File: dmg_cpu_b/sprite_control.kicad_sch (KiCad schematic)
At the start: 136 parts

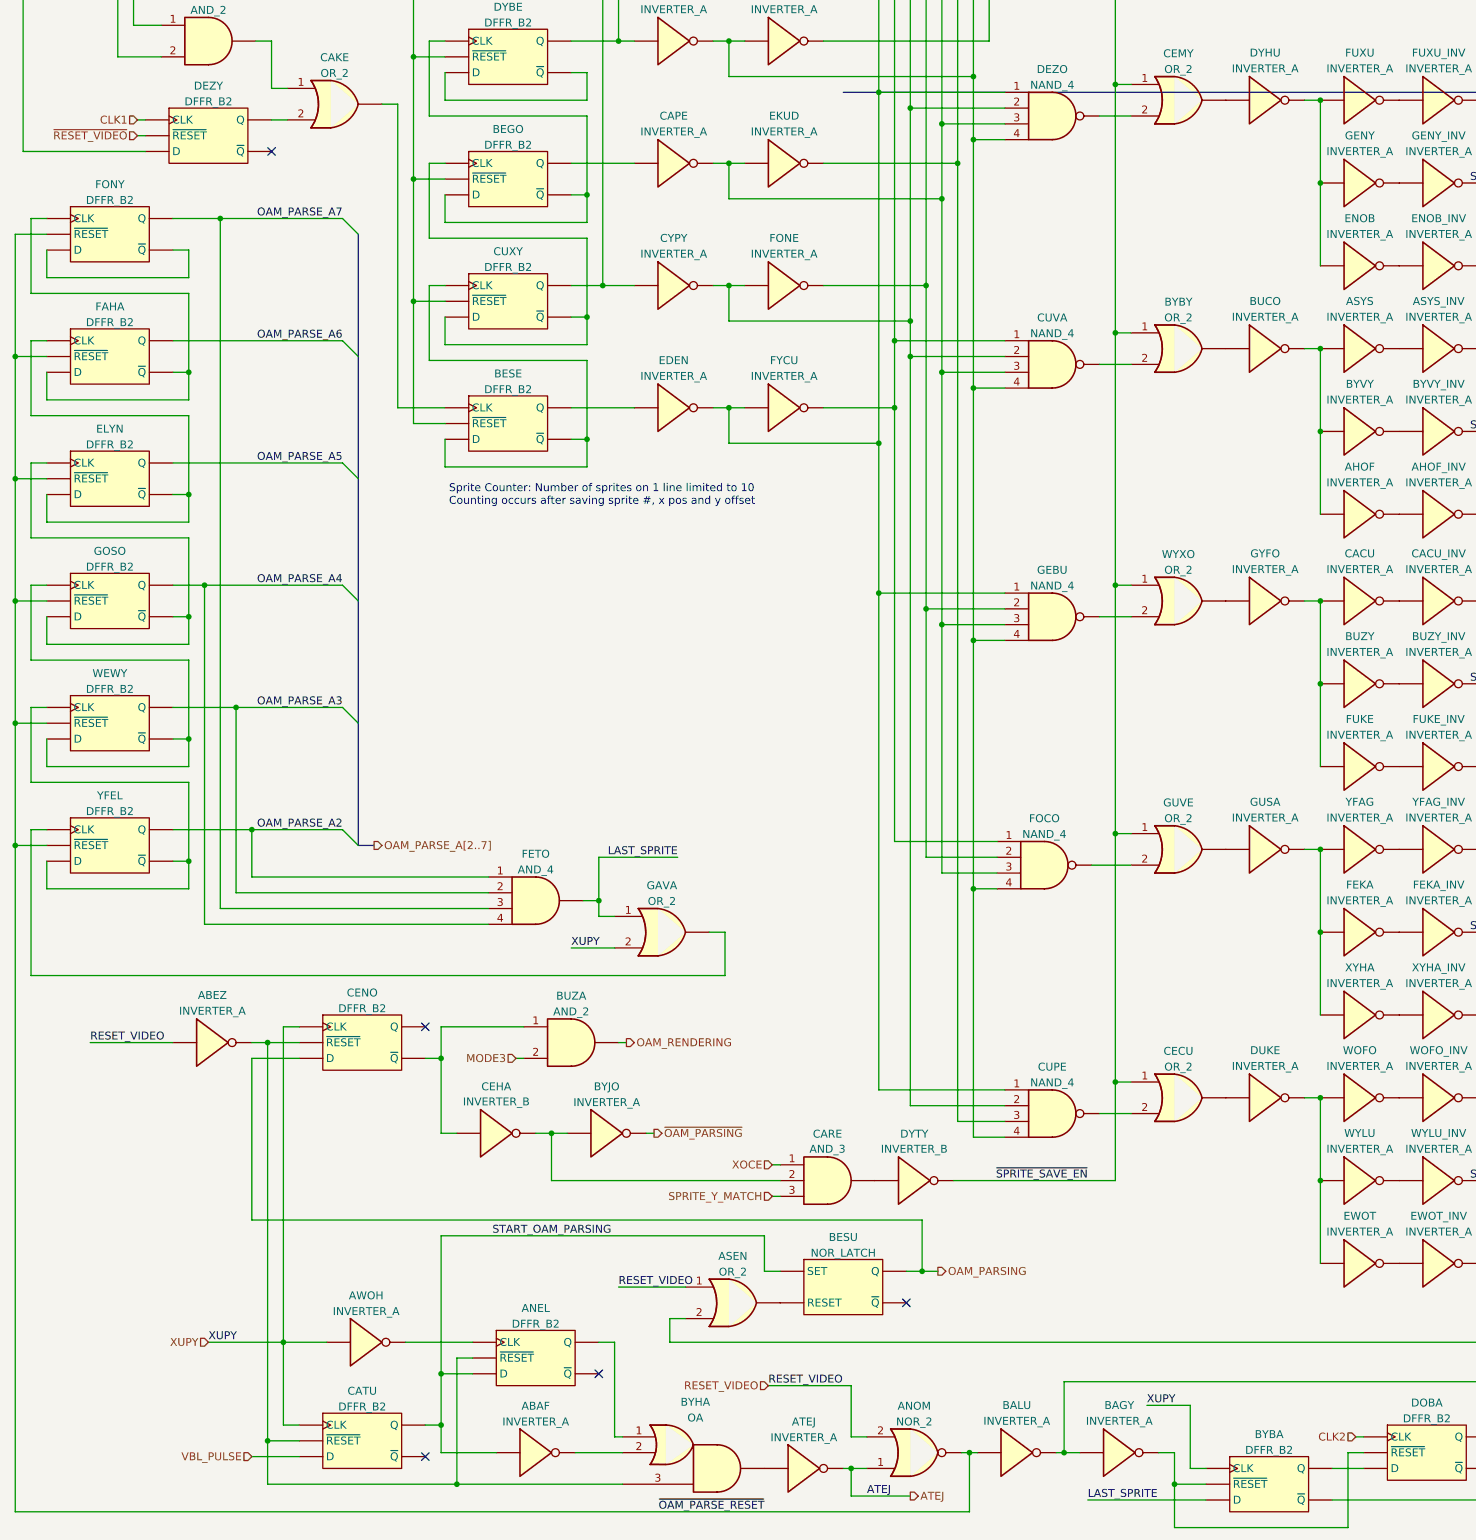
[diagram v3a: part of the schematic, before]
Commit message: PPU hierarchical page progress. Elements moved out of window sheet to be includes in BG and WIN cycles sheet
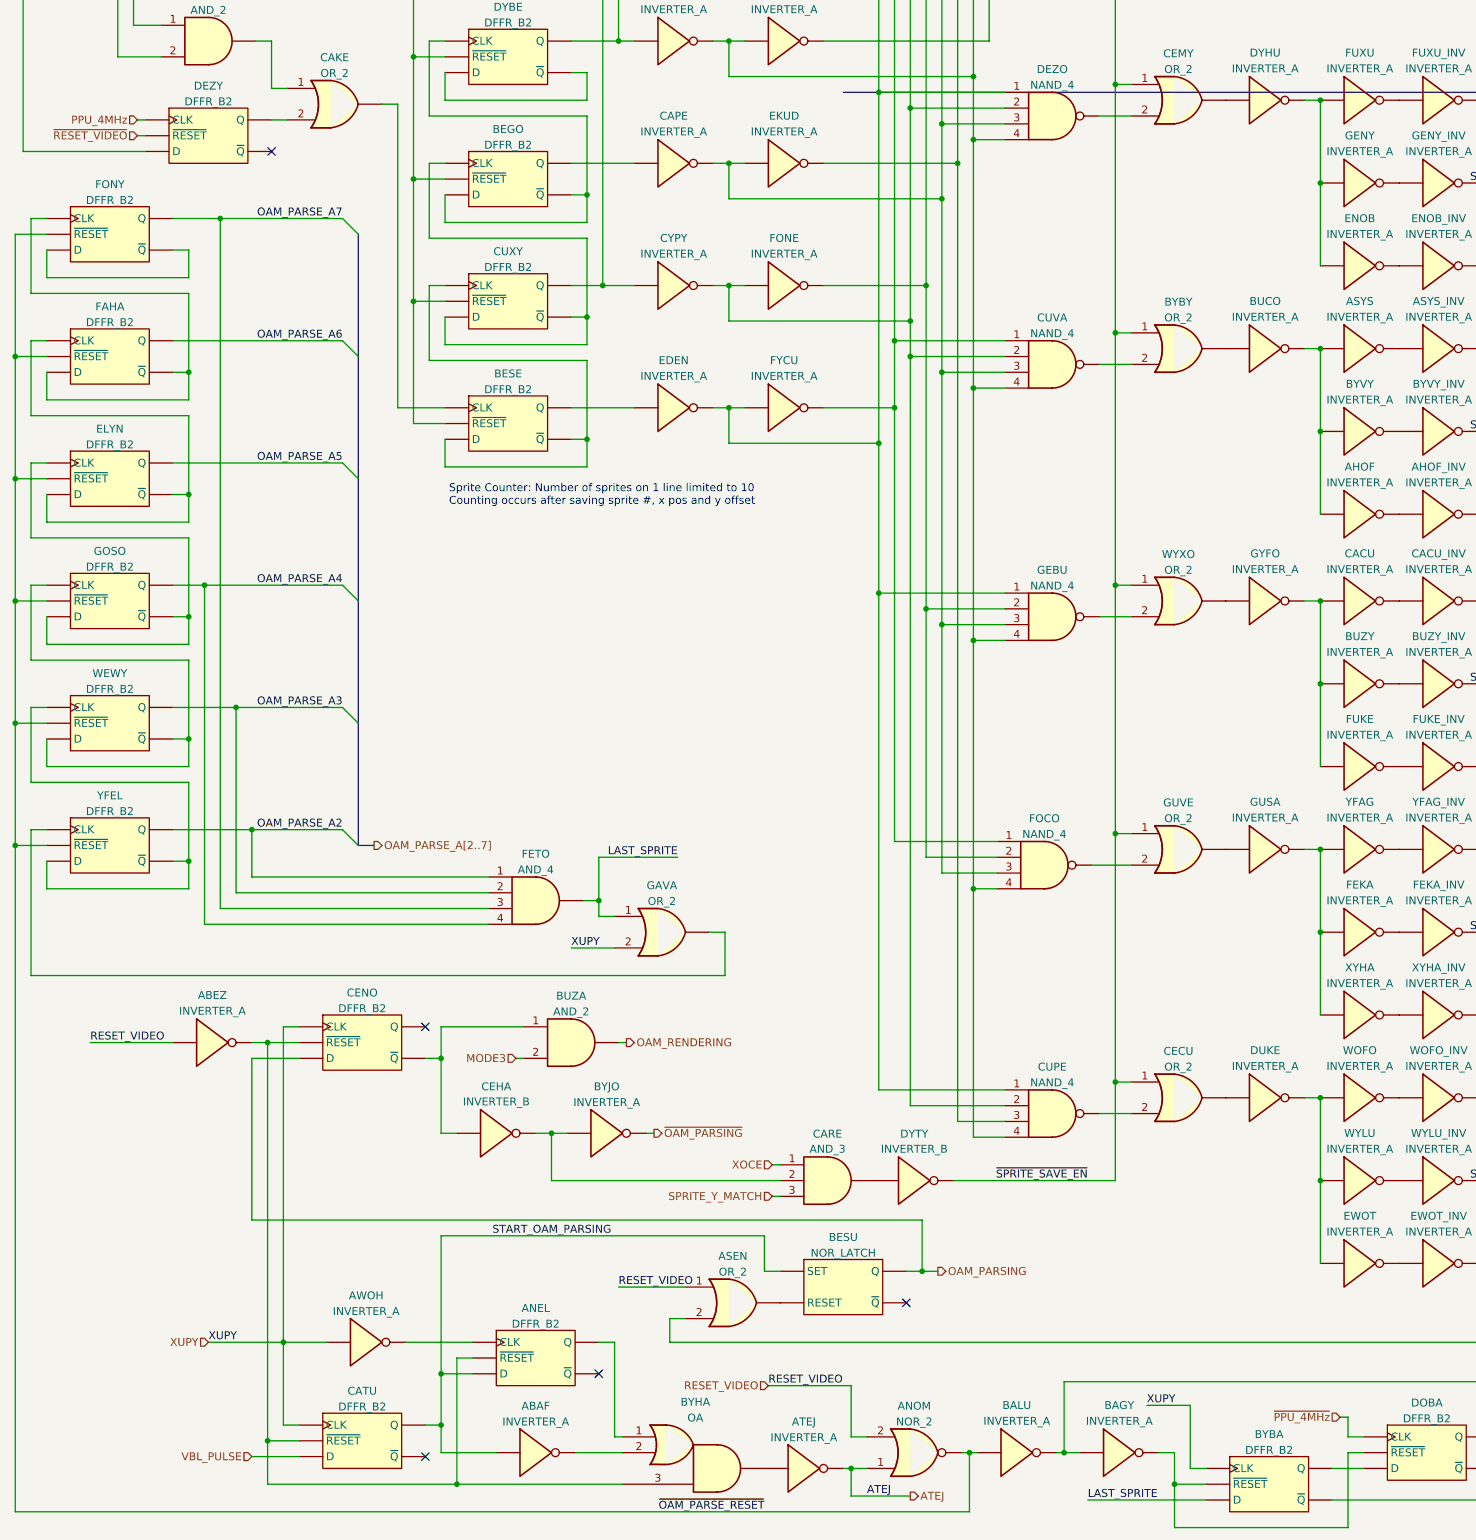
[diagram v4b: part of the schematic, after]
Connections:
- net CLK1 renamed PPU_4MHz
- net CLK2 renamed ~{PPU_4MHz}
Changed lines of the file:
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@@
     (stroke (width 0) (type default) (color 0 0 0 0))
   )
-  (wire (pts (xy 232.41 267.97) (xy 233.68 267.97))
+  (wire (pts (xy 229.87 264.795) (xy 231.14 264.795))
     (stroke (width 0) (type default) (color 0 0 0 0))
   )
@@
     (stroke (width 0) (type default) (color 0 0 0 0))
   )
+  (wire (pts (xy 231.14 267.97) (xy 233.68 267.97))
+    (stroke (width 0) (type default) (color 0 0 0 0))
+  )
   (wire (pts (xy 128.27 186.69) (xy 130.81 186.69))
     (stroke (width 0) (type default) (color 0 0 0 0))
@@
   )
   (bus (pts (xy 400.685 81.915) (xy 400.685 41.91))
+    (stroke (width 0) (type default) (color 0 0 0 0))
+  )
+  (wire (pts (xy 231.14 264.795) (xy 231.14 267.97))
     (stroke (width 0) (type default) (color 0 0 0 0))
   )
@@
     (effects (font (size 1.27 1.27)) (justify right))
   )
-  (hierarchical_label "CLK2" (shape input) (at 232.41 267.97 180)
+  (hierarchical_label "~{PPU_4MHz}" (shape input) (at 229.87 264.795 180)
     (effects (font (size 1.27 1.27)) (justify right))
   )
@@
     (effects (font (size 1.27 1.27)) (justify left))
   )
-  (hierarchical_label "CLK1" (shape input) (at 36.195 55.88 180)
+  (hierarchical_label "PPU_4MHz" (shape input) (at 36.195 55.88 180)
     (effects (font (size 1.27 1.27)) (justify right))
   )

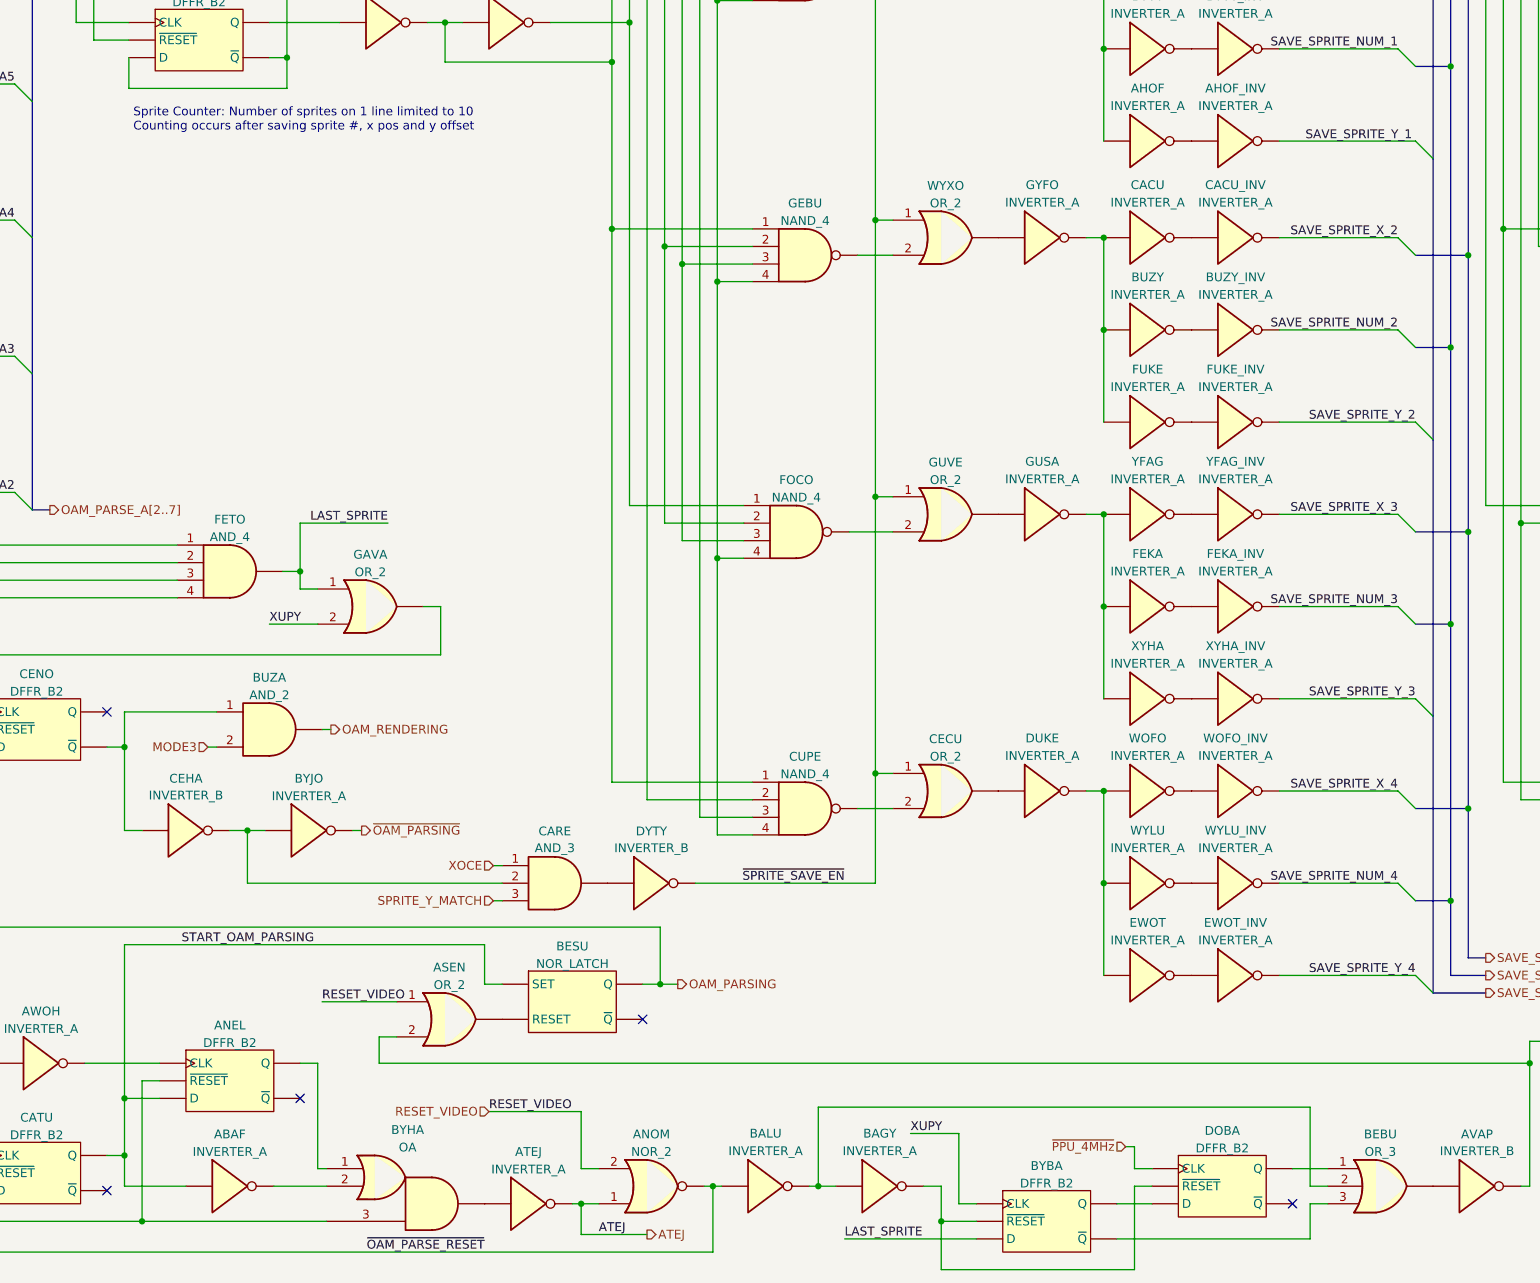
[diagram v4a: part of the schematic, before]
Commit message: All connections between sheet are complete. Can still do with a good tidy up.
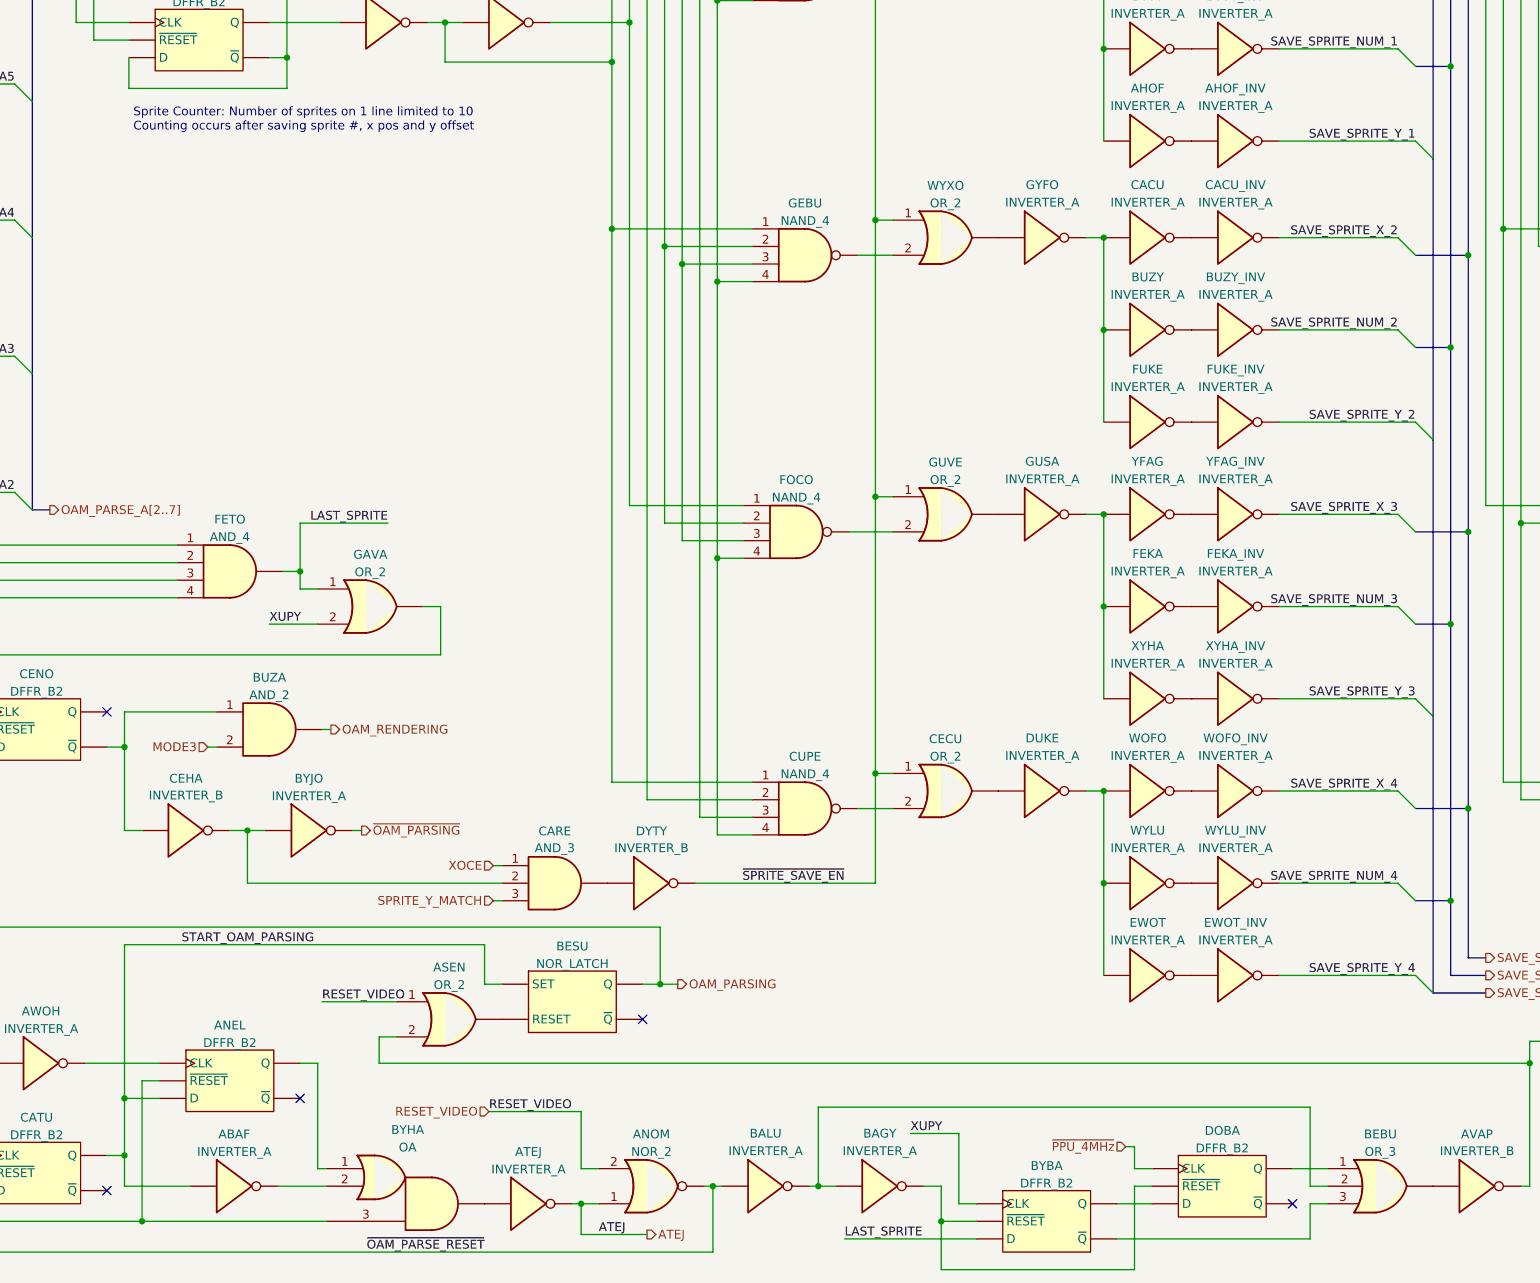
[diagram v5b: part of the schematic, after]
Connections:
- net SAVE_SPRITE_Y_1: now also AHOF_INV.2
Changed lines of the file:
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@@
     (stroke (width 0) (type default) (color 0 0 0 0))
   )
+  (wire (pts (xy 252.095 119.38) (xy 271.78 119.38))
+    (stroke (width 0) (type default) (color 0 0 0 0))
+  )
   (wire (pts (xy 287.02 174.625) (xy 287.02 214.63))
     (stroke (width 0) (type default) (color 0 0 0 0))
@@
     (stroke (width 0) (type default) (color 0 0 0 0))
   )
-  (wire (pts (xy 85.09 270.51) (xy 93.98 270.51))
+  (wire (pts (xy 85.09 270.51) (xy 94.615 270.51))
     (stroke (width 0) (type default) (color 0 0 0 0))
   )
@@
     (stroke (width 0) (type default) (color 0 0 0 0))
   )
-  (wire (pts (xy 106.68 270.51) (xy 114.3 270.51))
+  (wire (pts (xy 107.315 270.51) (xy 114.3 270.51))
     (stroke (width 0) (type default) (color 0 0 0 0))
   )
@@
     (stroke (width 0) (type default) (color 0 0 0 0))
   )
-  (wire (pts (xy 252.095 119.38) (xy 271.78 119.38))
-    (stroke (width 0) (type default) (color 0 0 0 0))
-  )
   (wire (pts (xy 297.18 99.06) (xy 302.26 99.06))
     (stroke (width 0) (type default) (color 0 0 0 0))
@@
     (effects (font (size 1.27 1.27)) (justify right bottom))
   )
-  (label "SAVE_SPRITE_Y_1" (at 271.2809 119.4605 180)
+  (label "SAVE_SPRITE_Y_1" (at 271.78 119.38 180)
     (effects (font (size 1.27 1.27)) (justify right bottom))
   )
@@
     (pin "6")
   )
+  (symbol (lib_id "DMG_CPU_Cells:INVERTER_A") (at 100.965 270.51 0) (unit 1)
+    (in_bom yes) (on_board yes) (fields_autoplaced)
+    (property "Reference" "ABAF" (id 0) (at 100.965 263.0002 0))
+    (property "Value" "INVERTER_A" (id 1) (at 100.965 265.5371 0))
+    (property "Footprint" "" (id 2) (at 98.425 270.51 0)
+      (effects (font (size 1.27 1.27)) hide)
+    )
+    (property "Datasheet" "http://iceboy.a-singer.de/doc/dmg_cells.html#inv_a" (id 3) (at 102.235 278.13 0)
+      (effects (font (size 1.27 1.27)) hide)
+    )
+    (pin "1")
+    (pin "2")
+  )
   (symbol (lib_id "DMG_CPU_Cells:INVERTER_A") (at 233.045 213.36 0) (unit 1)
     (in_bom yes) (on_board yes)
@@
       (effects (font (size 1.27 1.27)) hide)
     )
-    (pin "1")
-    (pin "2")
-  )
-  (symbol (lib_id "DMG_CPU_Cells:INVERTER_A") (at 100.33 270.51 0) (unit 1)
-    (in_bom yes) (on_board yes) (fields_autoplaced)
-    (property "Reference" "ABAF" (id 0) (at 100.33 263.0002 0))
-    (property "Value" "INVERTER_A" (id 1) (at 100.33 265.5371 0))
-    (property "Footprint" "" (id 2) (at 97.79 270.51 0)
-      (effects (font (size 1.27 1.27)) hide)
-    )
-    (property "Datasheet" "http://iceboy.a-singer.de/doc/dmg_cells.html#inv_a" (id 3) (at 101.6 278.13 0)
-      (effects (font (size 1.27 1.27)) hide)
-    )
